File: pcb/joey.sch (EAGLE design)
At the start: 62 parts, among them J1 AVR_SPI_PRG_6PTH, U1 ATMEGA168, U2 TMP102, X1 USB-MICROB, Y1 13.56M

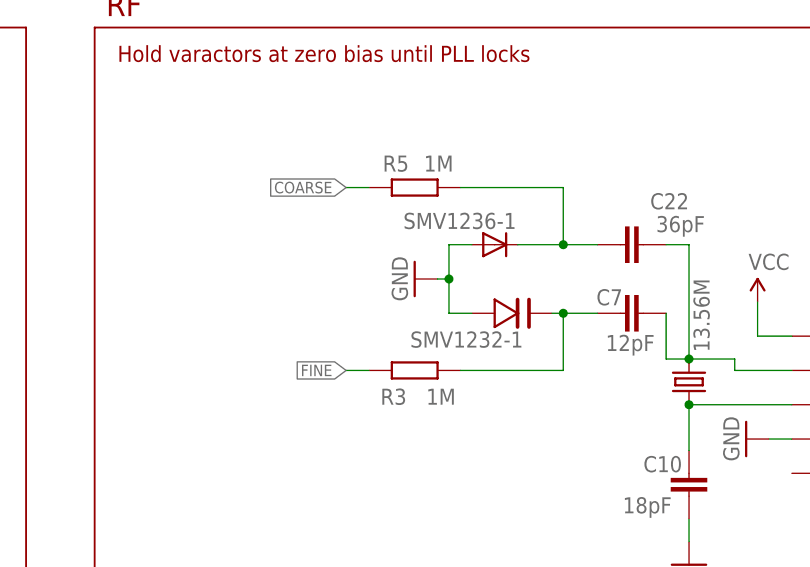
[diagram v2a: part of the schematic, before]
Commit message: Fixed the varactor grounding bug in v1.0
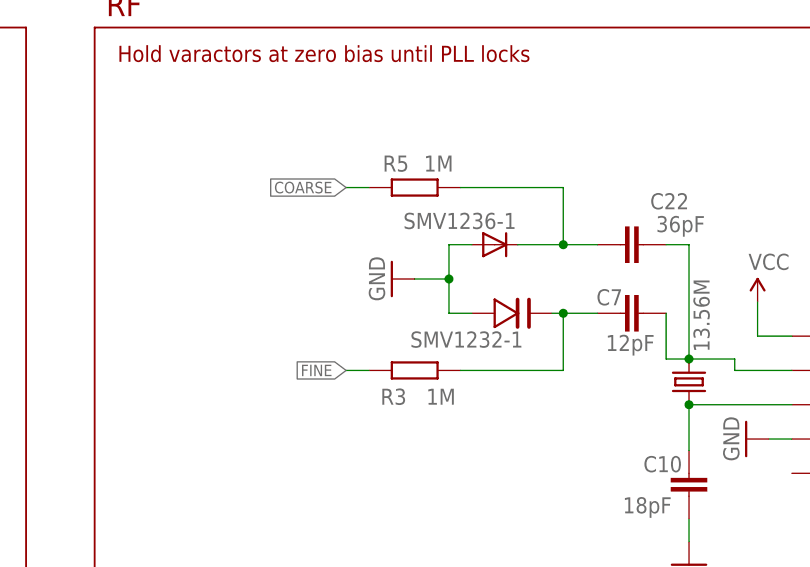
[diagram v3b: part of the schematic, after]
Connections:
- removed net SMV1247-1: SMV1232-1.ANODE, SMV1236-1.A
- net GND: now also SMV1232-1.ANODE, SMV1236-1.A
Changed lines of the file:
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@@
 <setting verticaltext="up"/>
 </settings>
-<grid distance="0.05" unitdist="inch" unit="inch" style="lines" multiple="1" display="no" altdistance="0.01" altunitdist="inch" altunit="inch"/>
+<grid distance="0.1" unitdist="inch" unit="inch" style="lines" multiple="1" display="no" altdistance="0.01" altunitdist="inch" altunit="inch"/>
 <layers>
 <layer number="1" name="Top" color="4" fill="1" visible="no" active="no"/>
@@
 <attribute name="NAME" x="59.182" y="7.62" size="1.778" layer="95"/>
 </instance>
-<instance part="GND8" gate="1" x="59.69" y="15.24" rot="R270"/>
+<instance part="GND8" gate="1" x="57.15" y="15.24" rot="R270"/>
 <instance part="C11" gate="G$1" x="144.78" y="8.89" smashed="yes" rot="R270">
 <attribute name="NAME" x="142.494" y="14.351" size="1.778" layer="95"/>
@@
 <wire x1="43.18" y1="-110.49" x2="40.64" y2="-110.49" width="0.1524" layer="91"/>
 <pinref part="GND35" gate="1" pin="GND"/>
+</segment>
+<segment>
+<wire x1="63.5" y1="19.05" x2="63.5" y2="15.24" width="0.1524" layer="91"/>
+<wire x1="63.5" y1="15.24" x2="63.5" y2="11.43" width="0.1524" layer="91"/>
+<wire x1="63.5" y1="11.43" x2="66.04" y2="11.43" width="0.1524" layer="91"/>
+<wire x1="63.5" y1="15.24" x2="59.69" y2="15.24" width="0.1524" layer="91"/>
+<wire x1="66.04" y1="19.05" x2="63.5" y2="19.05" width="0.1524" layer="91"/>
+<junction x="63.5" y="15.24"/>
+<pinref part="SMV1232-1" gate="G$1" pin="ANODE"/>
+<pinref part="GND8" gate="1" pin="GND"/>
+<pinref part="SMV1236-1" gate="G$1" pin="A"/>
 </segment>
 </net>
@@
 </segment>
 </net>
-<net name="SMV1247-1" class="0">
-<segment>
-<wire x1="63.5" y1="19.05" x2="63.5" y2="15.24" width="0.1524" layer="91"/>
-<wire x1="63.5" y1="15.24" x2="63.5" y2="11.43" width="0.1524" layer="91"/>
-<wire x1="63.5" y1="11.43" x2="66.04" y2="11.43" width="0.1524" layer="91"/>
-<wire x1="63.5" y1="15.24" x2="62.23" y2="15.24" width="0.1524" layer="91"/>
-<wire x1="66.04" y1="19.05" x2="63.5" y2="19.05" width="0.1524" layer="91"/>
-<junction x="63.5" y="15.24"/>
-<pinref part="SMV1232-1" gate="G$1" pin="ANODE"/>
-<pinref part="GND8" gate="1" pin="GND"/>
-<pinref part="SMV1236-1" gate="G$1" pin="A"/>
-</segment>
-</net>

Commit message: Finished rev2 of Joey, submission to CCC at this SHA1
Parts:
- removed U2: TMP102, SparkFun:TMP102
- added U$12: TMP100, jonsowman:TMP100
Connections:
- net GND: now also U$12.ADD0, U$12.GND; no longer U2.ADD0, U2.GND
- net I2C_SCL: now also U$12.SCL; no longer U2.SCL
- net I2C_SDA: now also U$12.SDA; no longer U2.SDA
- net VCC: now also U$12.VCC; no longer U2.VCC
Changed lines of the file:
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@@
 <?xml version="1.0" encoding="utf-8"?>
 <!DOCTYPE eagle SYSTEM "eagle.dtd">
-<eagle version="6.1">
+<eagle version="6.2">
 <drawing>
 <settings>
@@
 <setting verticaltext="up"/>
 </settings>
-<grid distance="0.1" unitdist="inch" unit="inch" style="lines" multiple="1" display="no" altdistance="0.01" altunitdist="inch" altunit="inch"/>
+<grid distance="0.05" unitdist="inch" unit="inch" style="lines" multiple="1" display="yes" altdistance="0.01" altunitdist="inch" altunit="inch"/>
 <layers>
 <layer number="1" name="Top" color="4" fill="1" visible="no" active="no"/>
@@
 <part name="R4" library="rcl" deviceset="R-EU_" device="R0603" value="100R"/>
 <part name="R6" library="rcl" deviceset="R-EU_" device="R0603" value="100R"/>
-<part name="U2" library="SparkFun" deviceset="TMP102" device=""/>
 <part name="R7" library="rcl" deviceset="R-EU_" device="R0603" value="4K7"/>
 <part name="R8" library="rcl" deviceset="R-EU_" device="R0603" value="4K7"/>
@@
 <part name="P+3" library="SparkFun" deviceset="VCC" device=""/>
 <part name="P+13" library="SparkFun" deviceset="VCC" device=""/>
+<part name="U$12" library="jonsowman" deviceset="TMP100" device=""/>
 </parts>
 <sheets>
@@
 <attribute name="VALUE" x="-1.778" y="-82.55" size="1.778" layer="96" rot="R90"/>
 </instance>
-<instance part="U2" gate="G$1" x="-19.05" y="-19.05"/>
 <instance part="R7" gate="G$1" x="-121.92" y="-158.75" smashed="yes" rot="R90">
 <attribute name="NAME" x="-117.0686" y="-165.1" size="1.778" layer="95" rot="R90"/>
@@
 <instance part="P+3" gate="1" x="52.07" y="-109.22"/>
 <instance part="P+13" gate="1" x="199.39" y="22.86"/>
+<instance part="U$12" gate="G$1" x="-19.05" y="-19.05"/>
 </instances>
 <busses>
@@
 </segment>
 <segment>
-<pinref part="U2" gate="G$1" pin="GND"/>
 <wire x1="-31.75" y1="-24.13" x2="-34.29" y2="-24.13" width="0.1524" layer="91"/>
 <pinref part="GND28" gate="1" pin="GND"/>
@@
 <wire x1="-34.29" y1="-22.86" x2="-34.29" y2="-24.13" width="0.1524" layer="91"/>
 <junction x="-34.29" y="-24.13"/>
-</segment>
-<segment>
-<pinref part="U2" gate="G$1" pin="ADD0"/>
+<pinref part="U$12" gate="G$1" pin="GND"/>
+</segment>
+<segment>
 <wire x1="-8.89" y1="-24.13" x2="-6.35" y2="-24.13" width="0.1524" layer="91"/>
 <pinref part="GND29" gate="1" pin="GND"/>
 <wire x1="-6.35" y1="-24.13" x2="-6.35" y2="-26.67" width="0.1524" layer="91"/>
+<pinref part="U$12" gate="G$1" pin="ADD0"/>
 </segment>
 <segment>
@@
 <pinref part="P+10" gate="1" pin="VCC"/>
 <wire x1="-34.29" y1="-11.43" x2="-34.29" y2="-13.97" width="0.1524" layer="91"/>
-<pinref part="U2" gate="G$1" pin="VCC"/>
 <wire x1="-34.29" y1="-13.97" x2="-31.75" y2="-13.97" width="0.1524" layer="91"/>
 <pinref part="C19" gate="G$1" pin="2"/>
 <wire x1="-34.29" y1="-15.24" x2="-34.29" y2="-13.97" width="0.1524" layer="91"/>
 <junction x="-34.29" y="-13.97"/>
+<pinref part="U$12" gate="G$1" pin="VCC"/>
 </segment>
 <segment>
@@
 </segment>
 <segment>
-<pinref part="U2" gate="G$1" pin="SDA"/>
 <wire x1="-8.89" y1="-13.97" x2="-6.35" y2="-13.97" width="0.1524" layer="91"/>
 <label x="-6.35" y="-13.97" size="1.27" layer="95" xref="yes"/>
+<pinref part="U$12" gate="G$1" pin="SDA"/>
 </segment>
 <segment>
@@
 </segment>
 <segment>
-<pinref part="U2" gate="G$1" pin="SCL"/>
 <wire x1="-8.89" y1="-16.51" x2="-6.35" y2="-16.51" width="0.1524" layer="91"/>
 <label x="-6.35" y="-16.51" size="1.27" layer="95" xref="yes"/>
-</segment>
-<segment>
+<pinref part="U$12" gate="G$1" pin="SCL"/>
+</segment>
+<segment>
